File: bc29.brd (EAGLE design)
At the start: 116.8 x 86.4 mm, 107 parts, among them J1 2520-5, Q1 IRF740, U1 LP2951, U10 MC14516B, U11 CD4053B, U12 HCF4520, U13 CD4013B, U14 CD4070B, U15 TSC900BIJA, U16 CD4060B, U17 MC14073B, U18 CD4070B, U19 CD4001B, U2 CD4081, U3 CD4023, U4 CD4093B, U5 MC14516B, U6 CD4013, U7 TLC27L41, U8 CD4013B, U9 CD4001B, X1 32.768KHz

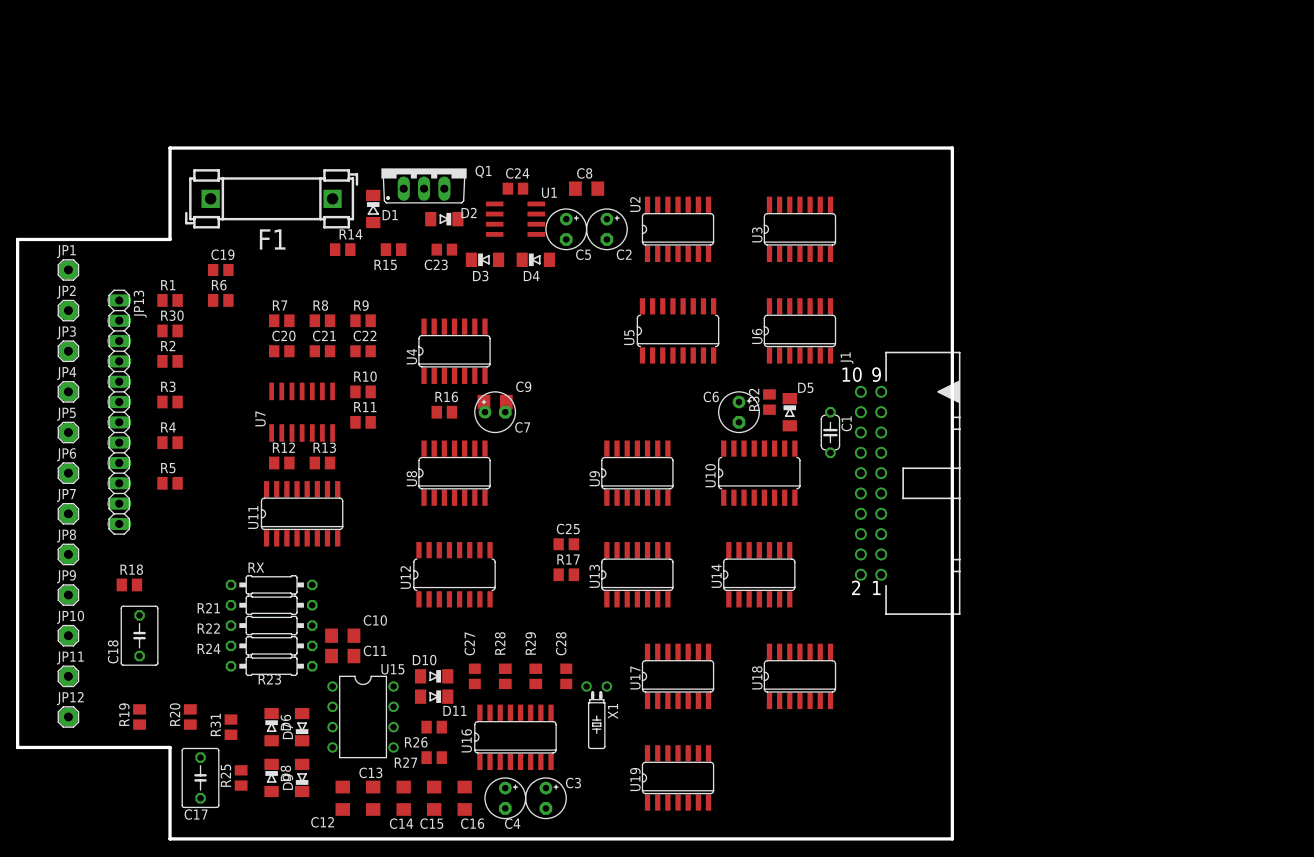
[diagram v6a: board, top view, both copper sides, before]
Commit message: Change reference designators and capacitor values to match 'Official' schematic
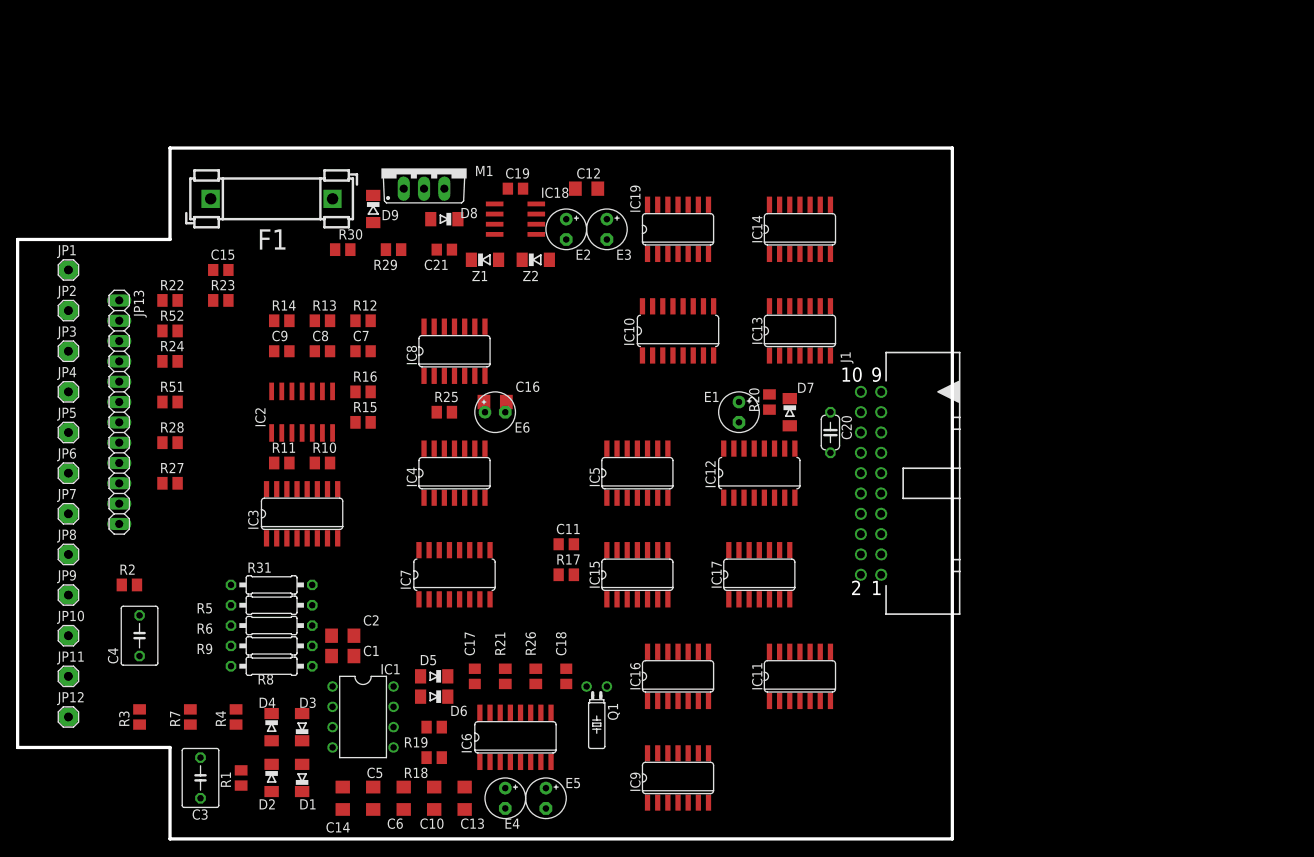
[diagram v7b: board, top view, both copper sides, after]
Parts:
- removed C22, C23, C24, C25, C27, C28: (no value), rcl:C0805
- removed D10, D11: 1n4148, diode:MINIMELF
- removed R32: 1K, rcl:M0805
- removed RX: OPEN, rcl:0207/10
- removed X1: 32.768KHz, crystal:TC26H
- added E1, E2, E6: 10uF 63V, rcl:E2,5-5
- added E3, E4, E5: 47uf 25V, rcl:E2,5-5
- added M1: IRF740, transistor-power:TO220BV
- added R51: 2K, rcl:M0805
- added R52: 1K, rcl:M0805
- added Z1: 12V, diode:SOD80C
- added Z2: 6.2V, diode:SOD80C
- C1: value (none) -> 100nF; device rcl:C050-024X044 -> rcl:C1206
- C10, C12, C13, C14, C16: value (none) -> 100nF
- C11: value (none) -> 220pF; device rcl:C1206 -> rcl:C0805
- C15, C8, C9: value (none) -> 10nF; device rcl:C1206 -> rcl:C0805
- C17: value (none) -> 10pF; device rcl:C050-045X075 -> rcl:C0805
- C18: value (none) -> 39pF; device rcl:C050-045X075 -> rcl:C0805
- C19: value (none) -> 10nF
- C2: value 47uf 25V -> 100nF; device rcl:E2,5-5 -> rcl:C1206
- C20: device rcl:C0805 -> rcl:C050-024X044
- C3, C4: value 47uf 25V -> 1uF; device rcl:E2,5-5 -> rcl:C050-045X075
- C5, C6: value 10uF 63V -> 100nF; device rcl:E2,5-5 -> rcl:C1206
- C7: value 10uF 63V -> 10nF; device rcl:E2,5-5 -> rcl:C0805
- D1: value V674 -> 1N4448; device diode:SOD80C -> diode:MINIMELF
- D2, D4, D7: value 1N4148 -> 1N4448
- D3, D5: value ZENER? -> 1N4448
- D6, D8: value 1n4148 -> 1N4448
- D9: value 1n4148 -> 1N4004; device diode:MINIMELF -> diode:SOD80C
- F1: value (none) -> 32mA
- Q1: value IRF740 -> 32.768KHz; device transistor-power:TO220BV -> crystal:TC26H
- R1: value 20K -> 620
- R10: value 1M -> 3K
- R12, R14: value 1M -> 330K
- R13: value 3K -> 330K
- R16: value 100K -> 1M
- R18, R19: value 300 -> 47
- R2: value 20K -> 300
- R20: value 2K -> 1K
- R21: value 130K -> 10M; device rcl:0207/10 -> rcl:M0805
- R22: value 130K -> 20K; device rcl:0207/10 -> rcl:M0805
- R23: value 4.70K -> 100K; device rcl:0207/10 -> rcl:M0805
- R24: value 8.20K -> 20K; device rcl:0207/10 -> rcl:M0805
- R25: value 620 -> 100K
- R26: value 47 -> 330K
- R27: value 47 -> 2K
- R28: value 10M -> 2K
- R29: value 330K -> 1M
- R3: value 2K -> 300
- R30: value 1K -> 1M
- R31: value 10K -> OPEN; device rcl:M0805 -> rcl:0207/10
- R4: value 2K -> 10K
- R5: value 2K -> 130K; device rcl:M0805 -> rcl:0207/10
- R6: value 100K -> 130K; device rcl:M0805 -> rcl:0207/10
- R7: value 330K -> 2K
- R8: value 330K -> 4.70K; device rcl:M0805 -> rcl:0207/10
- R9: value 330K -> 8.20K; device rcl:M0805 -> rcl:0207/10
- moved R20 82.4 mm to (94.0, 54.6)
- moved C12 82.1 mm to (71.1, 81.3), turned to 0 degrees
- moved C5 75.1 mm to (44.5, 5.08), turned to 90 degrees
- moved D2 73.1 mm to (31.8, 7.62), turned to 270 degrees
- moved D8 73.1 mm to (53.3, 77.5), turned to 180 degrees
- moved D7 72.6 mm to (96.5, 53.3), turned to 270 degrees
- moved D1 71.7 mm to (35.6, 7.62), turned to 90 degrees
- moved D9 71.7 mm to (44.5, 78.7), turned to 270 degrees
- moved C15 71.2 mm to (25.4, 71.1), turned to 0 degrees
- moved C20 69.3 mm to (101.6, 50.8), turned to 270 degrees
- moved Q1 68.3 mm to (72.4, 19.1), turned to 180 degrees
- moved D4 67.1 mm to (31.8, 14.0), turned to 270 degrees
- moved C1 67.1 mm to (40.6, 22.9), turned to 0 degrees
- moved C6 63.9 mm to (48.3, 5.08), turned to 90 degrees
- moved D3 62.7 mm to (35.6, 14.0), turned to 90 degrees
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- renumbered U1 to IC18, U10 to IC12, U11 to IC3, U12 to IC7, U13 to IC15, U14 to IC17, U15 to IC1, U16 to IC6, U17 to IC16, U18 to IC11, U19 to IC9, U2 to IC19, U3 to IC14, U4 to IC8, U5 to IC10, U6 to IC13, U7 to IC2, U8 to IC4, U9 to IC5
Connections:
- net !NAR: now also R22.1; no longer R1.1
- net !NAR_R: now also C15.1, R22.2, R23.1; no longer C19.1, R1.2, R6.1
- net !RESET: now also R24.1; no longer R2.1
- net +5V: now also C12.1, C19.1, E3.+, R11.2, R19.2, Z1.A, Z2.C; no longer C2.+, C24.1, C8.1, D3.A, D4.C, R12.2, R26.2
- net -1V25: now also C8.1, C9.2, R13.1, R14.2; no longer C20.2, C21.1, R7.2, R8.1
- net -2V5: now also C9.1, R14.1; no longer C20.1, R7.1
- net -2V5_BUF: now also R10.2; no longer R13.2
- net -2V5_BUF_R: now also R10.1; no longer R13.1
- net -4V: now also D6.A, E4.-; no longer C4.-, D11.A
- net -5V: now also C13.1, R18.1; no longer C16.1, R27.1
- net 0V0: now also C8.2, R12.1, R13.2; no longer C21.2, R8.2, R9.1
- net 13V5: now also D8.A, E2.+, M1.S; no longer C5.+, D2.A, Q1.S
- net 1V25: now also C7.2, R11.1, R12.2; no longer C22.2, R12.1, R9.2
- net 2_048KHZ: now also E5.+; no longer C3.+
- net 32_768KHZ: now also R21.1, R26.1; no longer R28.1, R29.1
- net AH_NEGATIVE: now also R51.1; no longer R3.1
- net AH_NEGATIVE_R: now also R23.2, R51.2; no longer R3.2, R6.2
- net CXA: now also C5.1; no longer C13.1
- net CXB: now also C6.1; no longer C14.1
- net DRAIN: now also D9.C, M1.D; no longer D1.C, Q1.D
- net FUSED_BATT+: now also D9.A, R30.2; no longer D1.A, R14.2
- net GATE: now also C21.1, D8.C, M1.G, R29.2, Z1.C; no longer C23.1, D2.C, D3.C, Q1.G, R15.2
- net GND: now also C10.2, C17.1, C18.1, C20.2, C21.2, C3.2, C4.2, C5.2, C6.2, C7.1, D1.C, D2.A, D3.C, D5.C, D7.A, E2.-, E3.-, E4.+, E6.-, R52.2, Z2.A; no longer C1.2, C17.2, C18.2, C2.-, C22.1, C23.2, C24.2, C27.1, C28.1, C4.+, C5.-, C7.-, C8.2, C9.2, D10.C, D5.A, D6.A, D7.C, D8.A, D9.C, R30.2
- net GND1K: now also R52.1; no longer R30.1
- net IN+: now also C3.1, D1.A, D2.C, R1.2; no longer C17.1, D8.C, D9.A, R25.2
- net IN-: now also C1.1, C2.1, D3.A, D4.C, R3.2, R31.2, R4.1, R5.2, R7.1, R8.2; no longer C10.1, C11.1, D6.C, D7.A, R19.2, R20.1, R21.2, R23.2, R31.1, RX.2
- net LCD-20: now also D7.C, E1.-; no longer C6.-, D5.C
- net LCD-3: now also C20.1; no longer C1.1
- net N$13: now also C11.2; no longer C25.2
- net N$24: now also C11.1; no longer C25.1
- net N$29: now also R29.1, R30.1; no longer R14.1, R15.1
- net N$32: now also R20.2; no longer R32.2
- net N$38: now also D5.A, D6.C, E5.-; no longer C3.-, D10.A, D11.C
- net N$39: now also C17.2, Q1.1, R26.2; no longer C27.2, R29.2, X1.1
- net N$40: now also C18.2, Q1.2, R21.2; no longer C28.2, R28.2, X1.2
- net N$42: now also R5.1, R6.2; no longer R21.1, R22.2
- net N$45: now also R8.1, R9.2; no longer R23.1, R24.2
- net N$48: now also R25.1; no longer R16.1
- net N$53: now also R15.2; no longer R11.2
- net N$54: now also E1.+, R20.1; no longer C6.+, R32.1
- net N$55: now also R16.1; no longer R10.1
- net N$56: now also R15.1; no longer R11.1
- net N$57: now also R16.2; no longer R10.2
- net OUT: now also C1.2, C2.2; no longer C10.2, C11.2
- net OUT+: now also R28.1; no longer R4.1
- net OUT+_R: now also R28.2; no longer R4.2
- net OUT-: now also R27.1; no longer R5.1
- net OUT-_R: now also R27.2; no longer R5.2
- net RESET_R: now also C16.1, E6.+, R24.2, R25.2; no longer C7.+, C9.1, R16.2, R2.2
- net SHUNT+: now also R2.1; no longer R18.1
- net SHUNT+FILTER: now also C4.1, R2.2, R3.1; no longer C18.1, R18.2, R19.1
- net SHUNT-: now also R1.1; no longer R25.1
- net VDD+: now also C10.1, R19.1; no longer C15.1, R26.1
- net VDD-: now also C14.1, R18.2; no longer C12.1, R27.2
- net X0: now also R31.1, R7.2, R9.1; no longer R20.2, R24.1, RX.1
- net Y0: now also R4.2, R6.1; no longer R22.1, R31.2

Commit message: update lcd interface portion
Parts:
- C20, C21: value (none) -> 10nF
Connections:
- net AH_NEGATIVE_R renamed MINUS_SIGN_ON
- net LCD-10 renamed LCD_ONE_MSD
- net LCD-11 renamed LCD_COLON
- net LCD-17 renamed !LCD_RESET
- net LCD-19 renamed LCD_45_HZ
- net LCD-20 renamed V_F_OUT
- net LCD-7 renamed LCD_DECIMAL_POINT
- net LCD-8 renamed LCD_MINUS_SIGN
- net LCD-9 renamed OVER_FLOW_UP
- net N$14 renamed IC3-11
- net U12-14 renamed IC7-14
- net U13-12 renamed IC15-12
- net U13-13 renamed OVER_FLOW
- net U13-3 renamed IC15-3
- net U17-2 renamed IC16-2
- net U3-6 renamed IC14-6
- net U4-3 renamed IC8-3
- net U5-7 renamed IC10-7
- net U6-5 renamed IC13-5
- net U9-4 renamed IC5-4
- removed net N$22: IC9.11, IC9.2
- removed net U14-1: IC17.1, IC9.4, IC9.9
- removed net VCC: IC3.16
- removed net VEE: IC3.7
- new net COLON_ON: IC17.1
- new net IC17-1: IC9.4, IC9.9
- net +5V: now also IC3.16
- net -5V: now also IC3.7
- net AH_NEGATIVE_LCD: now also IC9.11, IC9.2
